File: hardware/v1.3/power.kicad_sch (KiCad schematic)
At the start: 48 parts, among them U1 ECP5-CABGA256, U2 TLV62569DBV, U3 TLV62569DBV, U4 TLV62569DBV

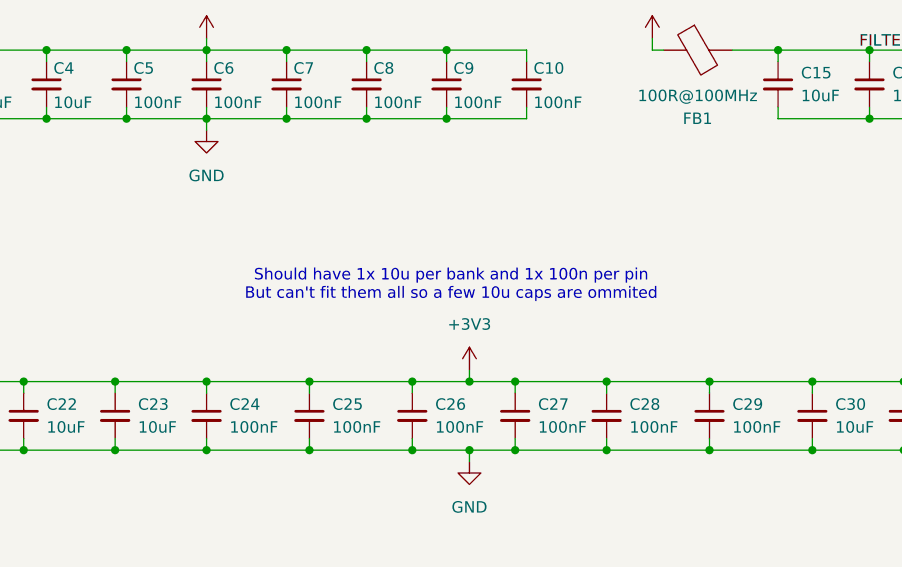
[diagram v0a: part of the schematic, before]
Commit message: QOL improvements on v1.3 PCB
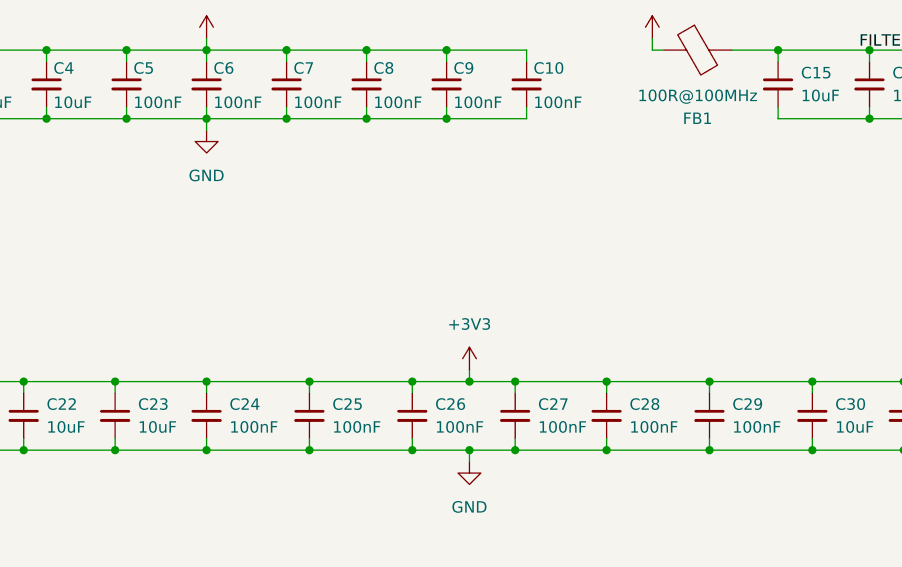
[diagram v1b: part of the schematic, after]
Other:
- note removed: "Should have 1x 10u per bank and 1x 100n per pin But can't fit them all so a few 10u caps are ommited"
